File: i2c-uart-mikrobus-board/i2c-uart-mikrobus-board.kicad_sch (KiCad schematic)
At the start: 9 parts, among them J1 mikroBUS_Board_L, J2 mikroBUS_Board_R, J3 Conn_02x08_Odd_Even, SW1 SW_Rotary4, SW2 SW_Rotary4, U1 SC16IS740IPW, Y1 1.8432MHz

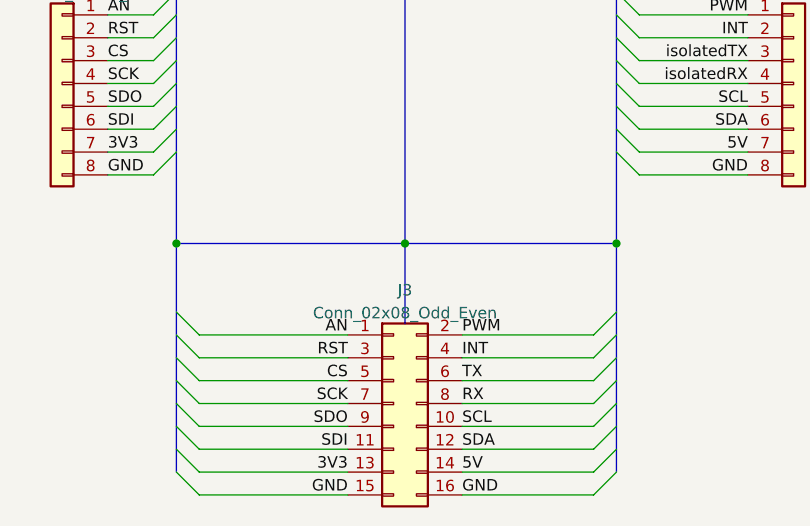
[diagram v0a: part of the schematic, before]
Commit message: i2c-spi-jumper-var2: add jumper to enable/disable ~INT pin connection
This allows mikroBUS boards like the OLED C click to be used with this
board without causing their Enable pin, which shares its location with the
~Interrupt pin, to be pulled low after SPI communication completes.
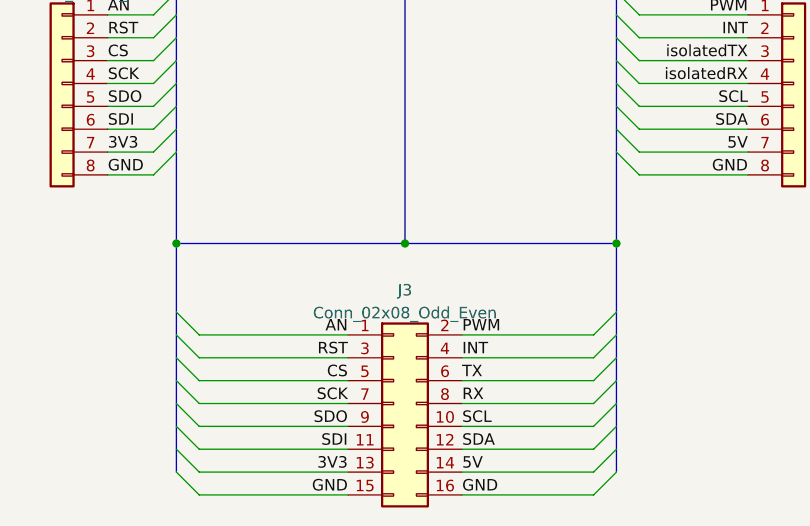
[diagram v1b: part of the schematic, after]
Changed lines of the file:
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@@
-    (stroke (width 0) (type default) (color 0 0 0 0))
-  )
-  (bus (pts (xy 135.89 139.7) (xy 135.89 148.59))
     (stroke (width 0) (type default) (color 0 0 0 0))
   )
